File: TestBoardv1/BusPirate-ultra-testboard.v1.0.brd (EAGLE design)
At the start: 40 x 45 mm, 24 parts, among them J1 CON_HEADER_1X10-RIGHT_ANGLED_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

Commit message: fix testboard IO header to match v1b, created gerbers
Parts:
- added LED15, LED16: (no value), dp_devices.v6:LED-805
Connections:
- removed net 3V3: J1.3, J1.4, LED10.A, LED12.A, LED2.A, LED4.A, LED6.A, LED8.A, R7.1
- removed net 5V0: J1.2, R8.1
- removed net ADC_DAC: J1.5, R6.1
- removed net AUX: J1.6, R5.1
- removed net CLOCK: J1.9, R2.1
- removed net CS: J1.7, R4.1
- removed net MISO: J1.8, R3.1
- removed net MOSI: J1.10, R1.1
- new net BPIO0: J1.1, R8.1
- new net BPIO1: J1.2, R7.1
- new net BPIO2: J1.3, R6.1
- new net BPIO3: J1.4, R5.1
- new net BPIO4: J1.5, R4.1
- new net BPIO5: J1.6, R3.1
- new net BPIO6: J1.7, R2.1
- new net BPIO7: J1.8, R1.1
- new net VOUT: J1.9, LED10.A, LED12.A, LED15.A, LED16.A, LED2.A, LED4.A, LED6.A, LED8.A
- net GND: now also J1.10; no longer J1.1
- net N$7: now also LED15.C
- net N$8: now also LED16.C
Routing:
- net 3V3: track 74.4 -> 0.00 mm, vias 7 -> 0
- net VOUT: track 0.00 -> 71.2 mm, vias 0 -> 8
- net BPIO7: track 0.00 -> 13.5 mm
- net 5V0: track 12.0 -> 0.00 mm, vias 1 -> 0
- net BPIO6: track 0.00 -> 11.6 mm
- net BPIO5: track 0.00 -> 9.14 mm
- net ADC_DAC: track 9.05 -> 0.00 mm, vias 1 -> 0
- net MOSI: track 8.89 -> 0.00 mm, vias 1 -> 0
- net BPIO0: track 0.00 -> 8.83 mm, vias 0 -> 1
- net BPIO4: track 0.00 -> 7.83 mm
- net AUX: track 6.74 -> 0.00 mm, vias 1 -> 0
- net CLOCK: track 6.68 -> 0.00 mm, vias 1 -> 0
- net BPIO1: track 0.00 -> 6.62 mm
- net CS: track 5.72 -> 0.00 mm, vias 1 -> 0
- net BPIO3: track 0.00 -> 5.72 mm
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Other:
- board text added: "BPIO-0"
- board text added: "BPIO-1"
- board text added: "BPIO-2"
- board text added: "BPIO-3"
- board text added: "BPIO-4"
- board text added: "BPIO-5"
- board text added: "BPIO-6"
- board text added: "BPIO-7"
- board text added: "SEP 2019"
- board text removed: "3.3V"
- board text removed: "5V"
- board text removed: "ADC/ DAC"
- board text removed: "AUX"
- board text removed: "CLOCK"
- board text removed: "CS"
- board text removed: "MAY 2019"
- board text removed: "MISO"
- board text removed: "MOSI"

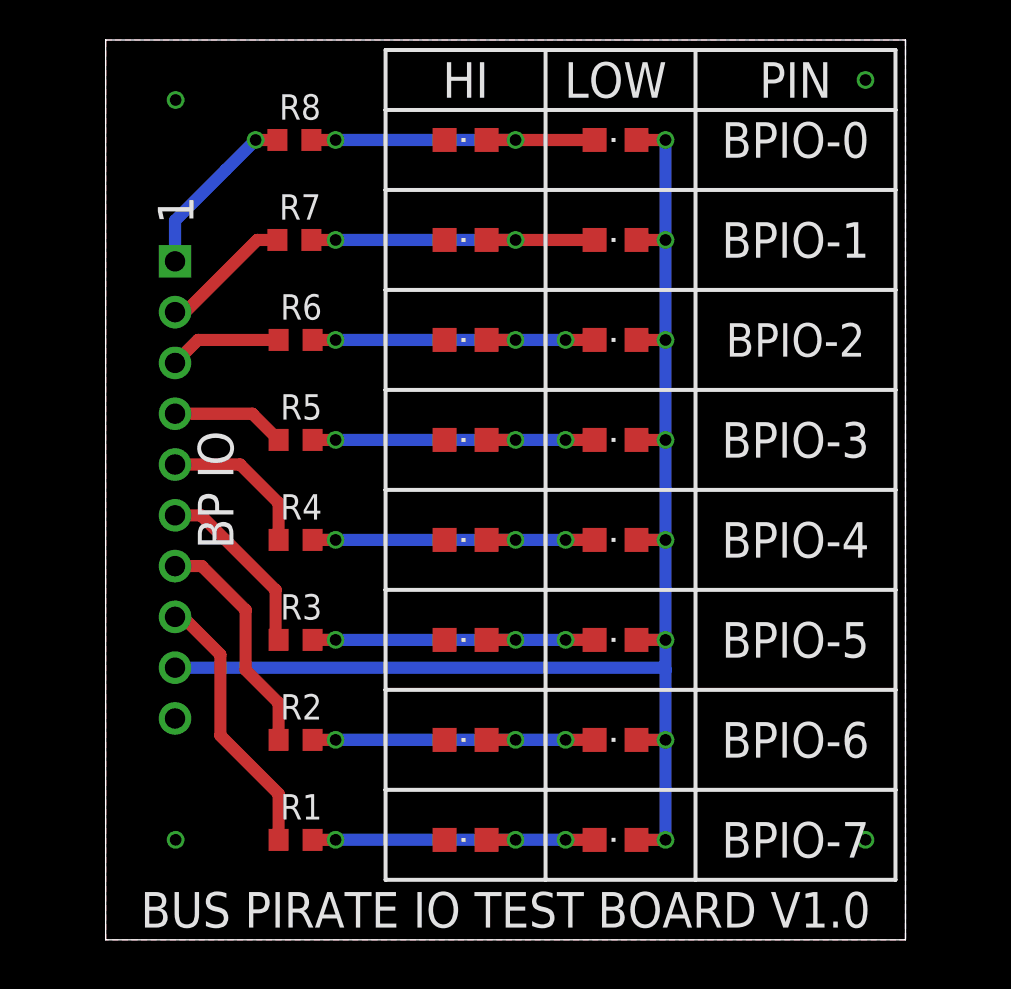
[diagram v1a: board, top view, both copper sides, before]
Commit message: added vout and GND test point. add LED status to vout
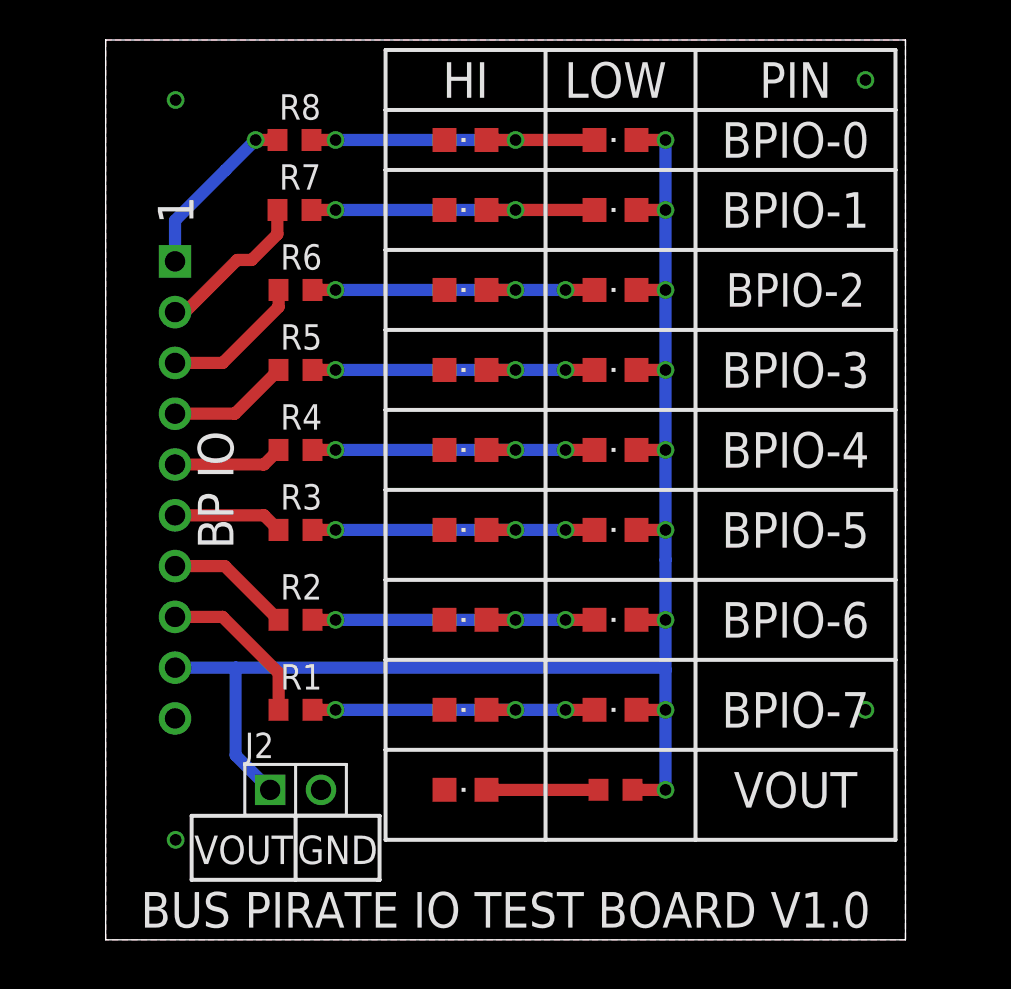
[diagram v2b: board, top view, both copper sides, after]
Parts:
- added J2: CON_HEADER_1X02-PTH, dp_devices.v6:M1X2
- added LED17: (no value), dp_devices.v6:LED-805
- added R9: 1k1, dp_devices.v6:R603
- moved LED1 6.50 mm to (18.0, 11.5)
- moved LED2 6.50 mm to (25.5, 11.5)
- moved R1 6.50 mm to (9.50, 11.5)
- moved LED3 6.00 mm to (18.0, 16.0)
- moved LED4 6.00 mm to (25.5, 16.0)
- moved R2 6.00 mm to (9.50, 16.0)
- moved LED5 5.50 mm to (18.0, 20.5)
- moved LED6 5.50 mm to (25.5, 20.5)
- moved R3 5.50 mm to (9.50, 20.5)
- moved LED7 4.50 mm to (18.0, 24.5)
- moved LED8 4.50 mm to (25.5, 24.5)
- moved R4 4.50 mm to (9.50, 24.5)
- moved LED10 3.50 mm to (25.5, 28.5)
- moved LED9 3.50 mm to (18.0, 28.5)
- moved R5 3.50 mm to (9.50, 28.5)
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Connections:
- new net N$9: LED17.A, R9.2
- net GND: now also J2.2, LED17.C
- net VOUT: now also J2.1, R9.1
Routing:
- net VOUT: track 71.2 -> 77.2 mm, vias 8 -> 9
- net N$9: track 0.00 -> 5.60 mm
- net BPIO7: track 13.5 -> 8.19 mm
- net BPIO6: track 11.6 -> 6.29 mm
- net BPIO5: track 9.14 -> 5.48 mm
- net BPIO4: track 7.83 -> 5.48 mm
- net BPIO2: track 5.66 -> 7.19 mm
- net BPIO1: track 6.62 -> 7.95 mm
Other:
- board text added: "GND"
- board text added: "VOUT"
